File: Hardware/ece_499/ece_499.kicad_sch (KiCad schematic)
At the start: 60 parts, among them J1 Conn_01x04, J2 Conn_01x04, J3 Conn_01x04, J4 Conn_01x04, J5 Conn_01x04, Q1 DMN2004WK, Q2 DMN2004WK, Q3 DMN2004WK, Q4 DMN2004WK, SW1 Encoder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

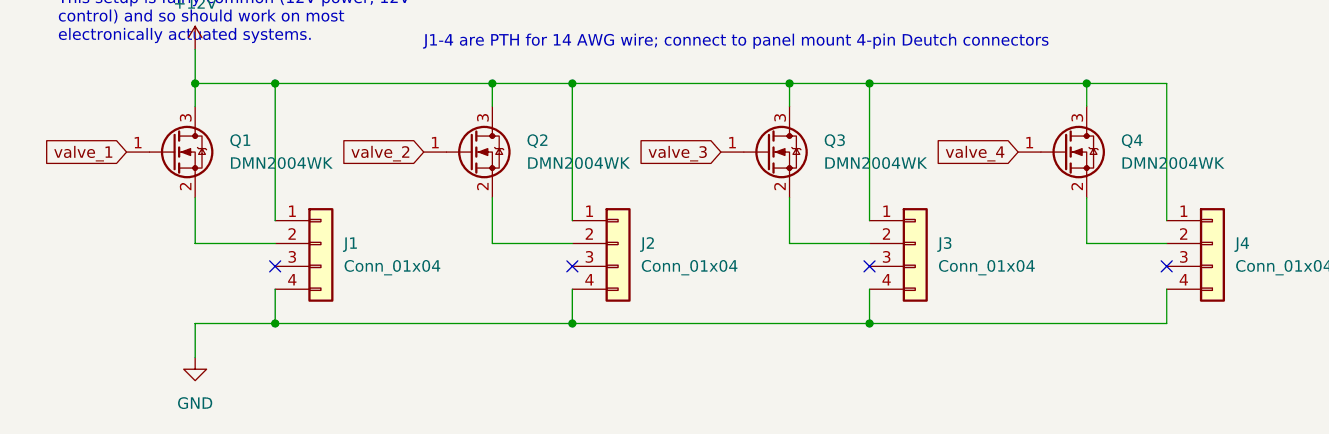
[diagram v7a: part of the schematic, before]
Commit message: Add pulldowns on valve FETs
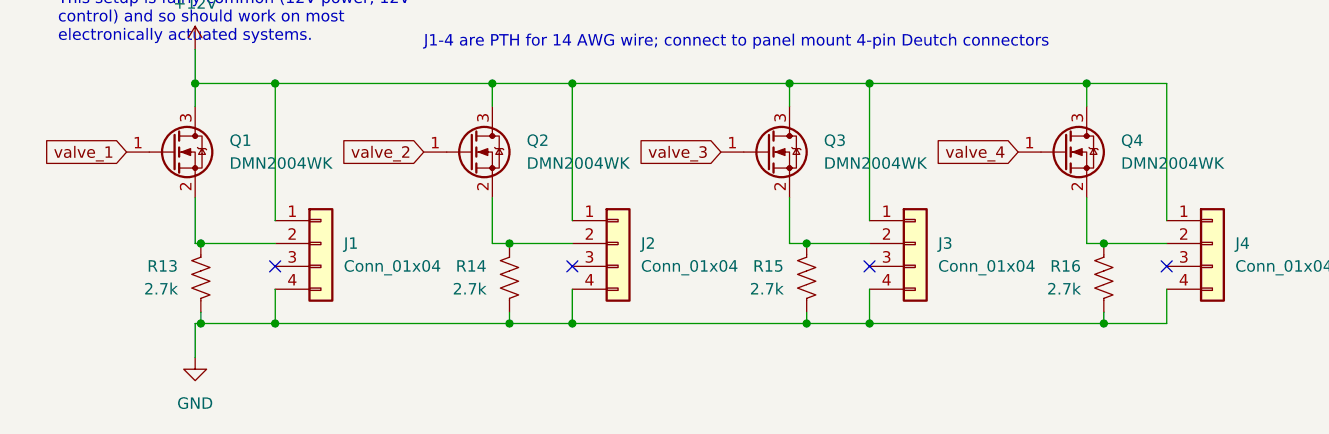
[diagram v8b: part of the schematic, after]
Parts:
- added R13, R14, R15, R16: 2.7k, Resistor_SMD:R_1206_3216Metric_Pad1.30x1.75mm_HandSolder, symbol Device:R_US
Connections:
- net GND: now also R13.1, R14.1, R15.1, R16.1
- net at J1.2 (Pin_2), Q1.2 (S): now also R13.2
- net at J3.2 (Pin_2), Q3.2 (S): now also R15.2
- net at J4.2 (Pin_2), Q4.2 (S): now also R16.2
- net at J2.2 (Pin_2), Q2.2 (S): now also R14.2
